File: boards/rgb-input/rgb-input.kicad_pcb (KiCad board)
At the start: 2 copper layers, 138.9 x 87 mm, 183 parts, among them J1 Barrel_Jack, J13 I2C, J42 INPUTS, J46 RGB, U1 ESP32-DEVKITC, U13 MCP1502, U15 MCP3425A0T-ECH, U2 MCP3208, U3 R-78K5.0-1.0, U5 TLC5947DAP, U6 TLC5947DAP

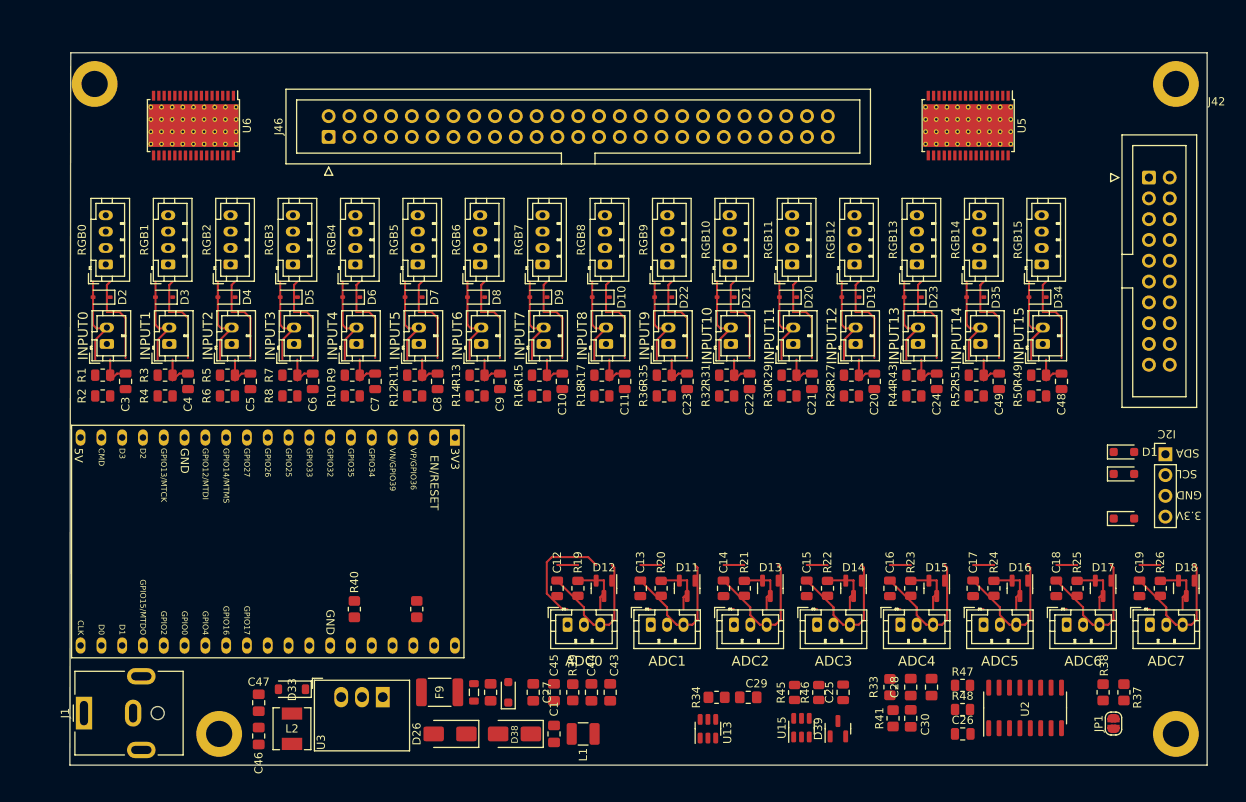
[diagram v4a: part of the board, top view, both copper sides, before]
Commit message: routed the rgb setup
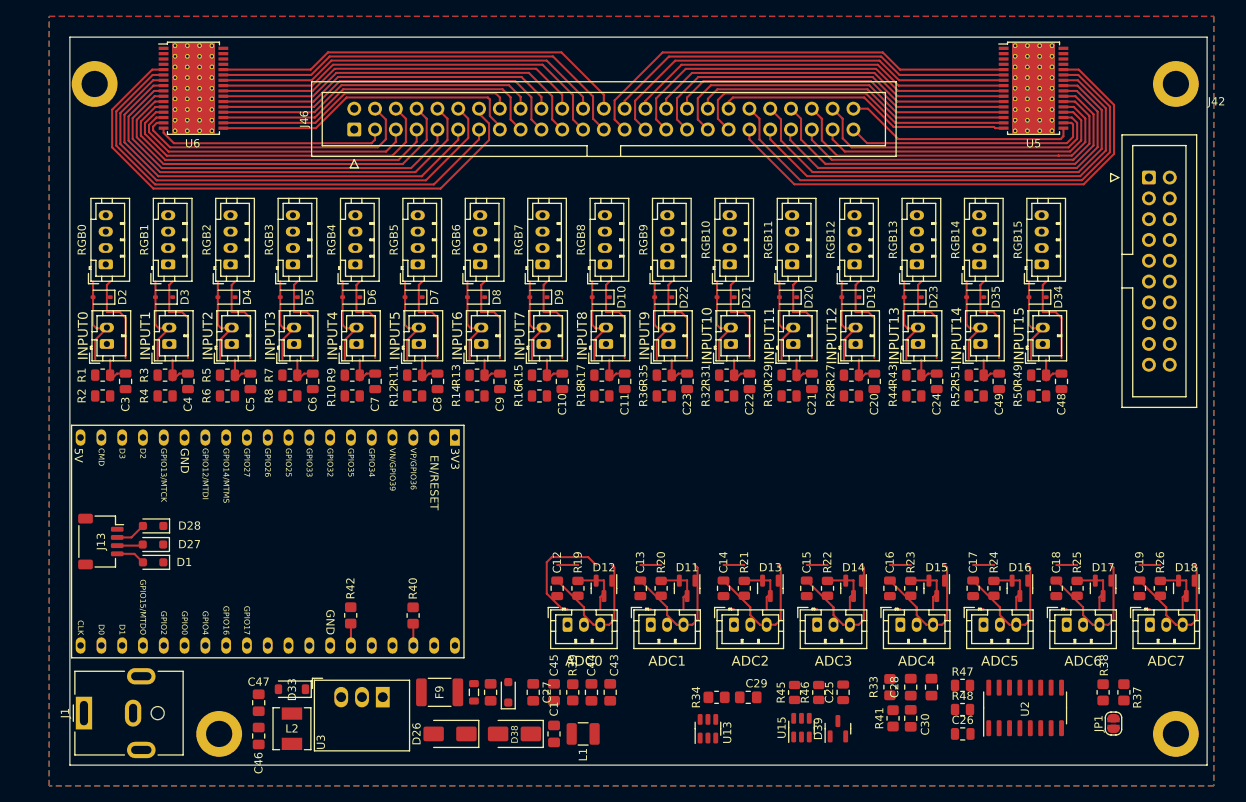
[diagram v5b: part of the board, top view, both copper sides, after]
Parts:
- J13: footprint Connector_PinHeader_2.54mm:PinHeader_1x04_P2.54mm_Vertical -> Connector_JST:JST_SH_SM04B-SRSS-TB_1x04-1MP_P1.00mm_Horizontal
- moved J13 130.4 mm to (78.8, 112.7), turned to -90 degrees
- moved D1 119.3 mm to (85.2, 115.2), turned to 180 degrees
- moved D27 118.9 mm to (85.1, 113.1), turned to 180 degrees
- moved D28 118.6 mm to (85.2, 110.8), turned to 180 degrees
- moved U5 9.19 mm to (192.7, 57.3), turned to 0 degrees
- moved R42 8.10 mm to (109.3, 121.7)
- moved R40 7.22 mm to (116.9, 121.7)
- moved U6 4.56 mm to (90.1, 57.3), turned to 0 degrees
- moved J46 3.26 mm to (109.7, 62.4)
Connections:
- D1 pad 2: SDA -> SCL
- D27 pad 2: SCL -> SDA
- J13 pad 1: SDA -> GNDD
- J13 pad 2: SCL -> +3.3V
- J13 pad 3: GNDD -> SDA
- J13 pad 4: +3.3V -> SCL
- J46 pad 10: /LEDS/GREEN2 -> /LEDS/GREEN1
- J46 pad 11: /LEDS/BLUE2 -> /LEDS/RED1
- J46 pad 12: /LEDS/RED3 -> /LEDS/BLUE0
- J46 pad 13: /LEDS/GREEN3 -> /LEDS/GREEN0
- J46 pad 14: /LEDS/BLUE3 -> /LEDS/RED0
- J46 pad 3: /LEDS/RED0 -> /LEDS/BLUE3
- J46 pad 39: /LEDS/RED12 -> /LEDS/BLUE15
- J46 pad 4: /LEDS/GREEN0 -> /LEDS/GREEN3
- J46 pad 40: /LEDS/GREEN12 -> /LEDS/GREEN15
- J46 pad 41: /LEDS/BLUE12 -> /LEDS/RED15
- J46 pad 42: /LEDS/RED13 -> /LEDS/BLUE14
- J46 pad 43: /LEDS/GREEN13 -> /LEDS/GREEN14
- J46 pad 44: /LEDS/BLUE13 -> /LEDS/RED14
- J46 pad 45: /LEDS/RED14 -> /LEDS/BLUE13
- J46 pad 46: /LEDS/GREEN14 -> /LEDS/GREEN13
- J46 pad 47: /LEDS/BLUE14 -> /LEDS/RED13
- J46 pad 48: /LEDS/RED15 -> /LEDS/BLUE12
- J46 pad 49: /LEDS/GREEN15 -> /LEDS/GREEN12
- J46 pad 5: /LEDS/BLUE0 -> /LEDS/RED3
- J46 pad 50: /LEDS/BLUE15 -> /LEDS/RED12
- J46 pad 6: /LEDS/RED1 -> /LEDS/BLUE2
- J46 pad 7: /LEDS/GREEN1 -> /LEDS/GREEN2
- J46 pad 8: /LEDS/BLUE1 -> /LEDS/RED2
- J46 pad 9: /LEDS/RED2 -> /LEDS/BLUE1
- R40 pad 1: SDA -> SCL
- R42 pad 1: SCL -> SDA
- RGB11 pad 2: /LEDS/RED12 -> /LEDS/RED11
- RGB11 pad 3: /LEDS/GREEN12 -> /LEDS/GREEN11
- RGB11 pad 4: /LEDS/BLUE12 -> /LEDS/BLUE11
- RGB12 pad 2: /LEDS/RED11 -> /LEDS/RED12
- RGB12 pad 3: /LEDS/GREEN11 -> /LEDS/GREEN12
- RGB12 pad 4: /LEDS/BLUE11 -> /LEDS/BLUE12
- RGB13 pad 2: /LEDS/RED14 -> /LEDS/RED13
- RGB13 pad 3: /LEDS/GREEN14 -> /LEDS/GREEN13
- RGB13 pad 4: /LEDS/BLUE14 -> /LEDS/BLUE13
- RGB14 pad 2: /LEDS/RED13 -> /LEDS/RED14
- RGB14 pad 3: /LEDS/GREEN13 -> /LEDS/GREEN14
- RGB14 pad 4: /LEDS/BLUE13 -> /LEDS/BLUE14
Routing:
- net /LEDS/RED0: track 0.00 -> 67.8 mm
- net /LEDS/BLUE15: track 0.00 -> 63.5 mm
- net /LEDS/GREEN15: track 0.00 -> 63.4 mm
- net /LEDS/GREEN0: track 0.00 -> 61.6 mm
- net /LEDS/BLUE0: track 0.00 -> 61.3 mm
- net /LEDS/RED15: track 0.00 -> 57.1 mm
- net /LEDS/BLUE14: track 0.00 -> 57.0 mm
- net /LEDS/RED1: track 0.00 -> 55.2 mm
- net /LEDS/GREEN1: track 0.00 -> 55.0 mm
- net /LEDS/RED8: track 0.00 -> 54.9 mm
- net /LEDS/GREEN7: track 0.00 -> 52.7 mm
- net /LEDS/BLUE8: track 0.00 -> 52.1 mm
- net /LEDS/BLUE7: track 0.00 -> 51.2 mm
- net /LEDS/GREEN14: track 0.00 -> 50.9 mm
- net /LEDS/RED14: track 0.00 -> 50.6 mm
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- added copper zone on B.Cu, net GNDD
- added copper zone on F.Cu, net GNDD
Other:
- board size 138.9 x 87 mm -> 138.9 x 88.9 mm
- board text removed: "3.3V"
- board text removed: "GND"
- board text removed: "I2C"
- board text removed: "SCL"
- board text removed: "SDA"

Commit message: so much routing.
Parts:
- removed R37: 0R, Resistor_SMD:R_0805_2012Metric_Pad1.20x1.40mm_HandSolder
- moved R47 127.3 mm to (83.4, 52.4), turned to 180 degrees
- moved R48 115.5 mm to (101.4, 52.5)
- moved R46 86.7 mm to (205.3, 53.6), turned to 0 degrees
- moved R45 81.1 mm to (183.0, 52.4), turned to 180 degrees
- moved J42 15.4 mm to (207.6, 83.6)
- moved H3 2.54 mm to (78.2, 54.3)
- moved U6 1.68 mm to (91.8, 57.3)
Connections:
- C25 pad 2: GND -> GNDD
- C26 pad 2: GND -> GNDD
- R45 pad 2: GND -> GNDD
- R46 pad 2: GND -> GNDD
- R47 pad 2: GND -> GNDD
- R48 pad 2: GND -> GNDD
- U5 pad 1: GND -> GNDD
- U5 pad 33: GND -> GNDD
- U6 pad 1: GND -> GNDD
- U6 pad 33: GND -> GNDD
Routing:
- net /LEDS/LED Driver/SOUT: track 0.00 -> 95.3 mm
- net /LEDS/BLUE4: track 41.4 -> 75.8 mm
- net /LEDS/BLUE6: track 50.0 -> 83.7 mm
- net /LEDS/RED0: track 67.8 -> 99.0 mm, vias 0 -> 1
- net /LEDS/RED4: track 38.4 -> 67.5 mm
- net /LEDS/RED1: track 55.2 -> 83.8 mm, vias 0 -> 1
- net /LEDS/GREEN4: track 36.8 -> 65.2 mm
- net /LEDS/RED2: track 48.6 -> 76.0 mm, vias 0 -> 1
- net /LEDS/RED3: track 36.2 -> 63.5 mm, vias 0 -> 1
- net /LEDS/GREEN0: track 61.6 -> 88.8 mm, vias 0 -> 1
- net /LEDS/RED5: track 39.7 -> 66.5 mm
- net /LEDS/GREEN1: track 55.0 -> 79.9 mm, vias 0 -> 1
- net /LEDS/GREEN3: track 35.9 -> 60.6 mm, vias 0 -> 1
- net /LEDS/GREEN2: track 42.6 -> 66.6 mm, vias 0 -> 1
- net /LEDS/BLUE0: track 61.3 -> 84.4 mm, vias 0 -> 1
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
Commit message: too much routing
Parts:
- removed C27: 1nF, Capacitor_SMD:C_0805_2012Metric_Pad1.18x1.45mm_HandSolder
- removed C28: 100nF, Capacitor_SMD:C_0805_2012Metric_Pad1.18x1.45mm_HandSolder
- removed C37: 10uF, Capacitor_SMD:C_0805_2012Metric_Pad1.18x1.45mm_HandSolder
- removed C46: 22nF, Capacitor_SMD:C_0805_2012Metric_Pad1.18x1.45mm_HandSolder
- removed D39: BAT54S, Package_TO_SOT_SMD:SOT-23
- removed R33: 300K 0.1%, Resistor_SMD:R_0805_2012Metric_Pad1.20x1.40mm_HandSolder
- removed R34: 22K 0.1%, Resistor_SMD:R_0805_2012Metric_Pad1.20x1.40mm_HandSolder
- removed U15: MCP3425A0T-ECH, Package_TO_SOT_SMD:SOT-23-6
- C47: value 47uF/6.3v -> 100uF/10v; footprint Capacitor_SMD:C_0805_2012Metric_Pad1.18x1.45mm_HandSolder -> Capacitor_Tantalum_SMD:CP_EIA-3528-21_Kemet-B
- L2: value SMMS0650-470M -> SMMS0650-680M
- U3: value R-78K5.0-1.0 -> XL1509-5.0; footprint gnarboard:RECOM R-78K -> Package_SO:SOIC-8_3.9x4.9mm_P1.27mm
- moved C25 105.6 mm to (101.4, 50.3), turned to 0 degrees
- moved C26 86.4 mm to (205.0, 52.4)
- moved R38 45.1 mm to (157.6, 119.7), turned to -90 degrees
- moved C43 42.1 mm to (99.4, 137.5)
- moved C44 42.1 mm to (97.1, 137.5)
- moved R39 39.4 mm to (97.1, 133.4)
- moved C1 33.9 mm to (100.4, 133.1), turned to 180 degrees
- moved C45 33.1 mm to (101.7, 137.5)
- moved L1 33.0 mm to (104.7, 137.2), turned to -90 degrees
- moved U13 30.5 mm to (177.9, 118.0), turned to 180 degrees
- moved U2 28.4 mm to (166.4, 119.9)
- moved F9 27.6 mm to (92.5, 130.1)
- moved JP1 27.4 mm to (177.9, 122.9), turned to 180 degrees
- moved FB7 27.3 mm to (97.1, 129.3)
- moved C2 27.0 mm to (99.4, 129.3)
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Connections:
- U1 pad 10: /INPUT7 -> /INPUT4
- U1 pad 11: /INPUT8 -> /INPUT3
- U1 pad 12: /INPUT9 -> /INPUT2
- U1 pad 13: /INPUT10 -> /INPUT1
- U1 pad 15: /INPUT11 -> /INPUT0
- U1 pad 3: /INPUT0 -> /INPUT11
- U1 pad 4: /INPUT1 -> /INPUT10
- U1 pad 5: /INPUT2 -> /INPUT9
- U1 pad 6: /INPUT3 -> /INPUT8
- U1 pad 7: /INPUT4 -> /INPUT7
- U1 pad 8: /INPUT5 -> /INPUT6
- U1 pad 9: /INPUT6 -> /INPUT5
- U3 pad 2: GNDD -> Net-(D33-K)
- U3 pad 3: Net-(D33-K) -> +5V
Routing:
- net GNDD: track 338.0 -> 20.5 mm, vias 6 -> 15
- net ESP32_VIN: track 0.00 -> 87.5 mm
- net /INPUT11: track 4.76 -> 54.4 mm
- net +5V: track 0.00 -> 47.2 mm
- net /INPUT10: track 4.76 -> 49.1 mm
- net /INPUT9: track 4.76 -> 44.1 mm
- net /LEDS/BLUE12: track 37.5 -> 75.7 mm, vias 0 -> 1
- net /LEDS/RED13: track 37.8 -> 75.0 mm, vias 0 -> 1
- net /LEDS/GREEN13: track 44.2 -> 80.8 mm, vias 0 -> 1
- net /INPUT8: track 4.76 -> 38.8 mm
- net /LEDS/RED14: track 50.6 -> 82.8 mm, vias 0 -> 1
- net /LEDS/BLUE13: track 44.3 -> 76.2 mm, vias 0 -> 1
- net Net-(U3-VIN): track 0.00 -> 30.9 mm
- net /INPUT7: track 4.76 -> 33.6 mm
- net /LEDS/GREEN14: track 50.9 -> 79.1 mm, vias 0 -> 1
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
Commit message: whoa, board is fully routed!!!!
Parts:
- moved LOGO 177.1 mm to (134.7, 103.9)
- moved J42 23.0 mm to (209.4, 113.3), turned to 180 degrees
- moved J1 10.7 mm to (87.4, 133.4), turned to -90 degrees
- moved R38 2.84 mm to (155.0, 118.4), turned to 180 degrees
- moved H4 2.73 mm to (210.6, 54.1)
- moved C25 2.41 mm to (101.4, 52.8)
- moved R48 2.29 mm to (101.4, 54.8)
- moved D27 1.04 mm to (86.2, 113.1)
- moved D1 1.02 mm to (86.2, 115.2)
- moved D28 1.02 mm to (86.2, 110.8)
- moved C29 0.92 mm to (173.6, 117.4), turned to -90 degrees
- moved H2 0.76 mm to (210.6, 136.7)
- moved H1 0.51 mm to (92.5, 136.7)
- renumbered REF** to LOGO
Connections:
- ADC0 pad 2: GNDD -> GNDA
- ADC1 pad 2: GNDD -> GNDA
- ADC2 pad 2: GNDD -> GNDA
- ADC3 pad 2: GNDD -> GNDA
- ADC4 pad 2: GNDD -> GNDA
- ADC5 pad 2: GNDD -> GNDA
- ADC6 pad 2: GNDD -> GNDA
- ADC7 pad 2: GNDD -> GNDA
- C12 pad 2: GNDD -> GNDA
- C13 pad 2: GNDD -> GNDA
- C14 pad 2: GNDD -> GNDA
- C15 pad 2: GNDD -> GNDA
- C16 pad 2: GNDD -> GNDA
- C17 pad 2: GNDD -> GNDA
- C18 pad 2: GNDD -> GNDA
- C19 pad 2: GNDD -> GNDA
- C29 pad 1: ESP32_5V -> +5V
- D11 pad 1: GNDD -> GNDA
- D12 pad 1: GNDD -> GNDA
- D13 pad 1: GNDD -> GNDA
- D14 pad 1: GNDD -> GNDA
- D15 pad 1: GNDD -> GNDA
- D16 pad 1: GNDD -> GNDA
- D17 pad 1: GNDD -> GNDA
- D18 pad 1: GNDD -> GNDA
- R10 pad 1: +3V3 -> +3.3V
- R12 pad 1: +3V3 -> +3.3V
- R14 pad 1: +3V3 -> +3.3V
- R16 pad 1: +3V3 -> +3.3V
- R18 pad 1: +3V3 -> +3.3V
- R2 pad 1: +3V3 -> +3.3V
- R28 pad 1: +3V3 -> +3.3V
- R30 pad 1: +3V3 -> +3.3V
- R32 pad 1: +3V3 -> +3.3V
- R36 pad 1: +3V3 -> +3.3V
- R4 pad 1: +3V3 -> +3.3V
- R44 pad 1: +3V3 -> +3.3V
- R50 pad 1: +3V3 -> +3.3V
- R52 pad 1: +3V3 -> +3.3V
- R6 pad 1: +3V3 -> +3.3V
- R8 pad 1: +3V3 -> +3.3V
- U1 pad 23: unconnected-(U1-GPIO15-Pad23) -> LED_SS
- U1 pad 28: SS -> ADC_SS
- U13 pad 4: ESP32_5V -> +5V
- U13 pad 6: ESP32_5V -> +5V
- U2 pad 10: SS -> ADC_SS
- U5 pad 29: /LEDS/LED Driver1/SOUT -> MISO
- U5 pad 30: SS -> LED_SS
- U6 pad 30: SS -> LED_SS
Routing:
- net +3.3V: track 11.0 -> 534.8 mm, vias 2 -> 24
- net LED_SS: track 0.00 -> 322.5 mm, vias 0 -> 4
- net SCK: track 13.7 -> 322.3 mm, vias 2 -> 5
- net +5V: track 47.2 -> 343.3 mm, vias 0 -> 3
- net MOSI: track 3.75 -> 222.3 mm, vias 1 -> 3
- net +3V3: track 0.00 -> 213.0 mm
- net MISO: track 0.00 -> 202.8 mm, vias 0 -> 4
- net /INPUT12: track 4.23 -> 188.8 mm, vias 0 -> 1
- net /INPUT13: track 4.23 -> 171.3 mm, vias 0 -> 1
- net /INPUT14: track 4.23 -> 168.4 mm, vias 0 -> 1
- net /INPUT15: track 4.23 -> 149.8 mm, vias 0 -> 1
- net /INPUT0: track 12.4 -> 143.0 mm, vias 0 -> 2
- net /INPUT1: track 11.0 -> 134.3 mm, vias 0 -> 2
- net /INPUT2: track 9.75 -> 128.0 mm, vias 0 -> 2
- net /INPUT3: track 12.3 -> 125.6 mm, vias 0 -> 2
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- added copper zone on B.Cu, net GNDA
- added copper zone on F.Cu, net GNDA
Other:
- board size 138.9 x 88.9 mm -> 138.9 x 89.2 mm
- board text added: "RGB I/O Board Rev A"
- board text removed: "8ch Mosfet Rev B"
